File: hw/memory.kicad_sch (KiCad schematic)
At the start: 5 parts

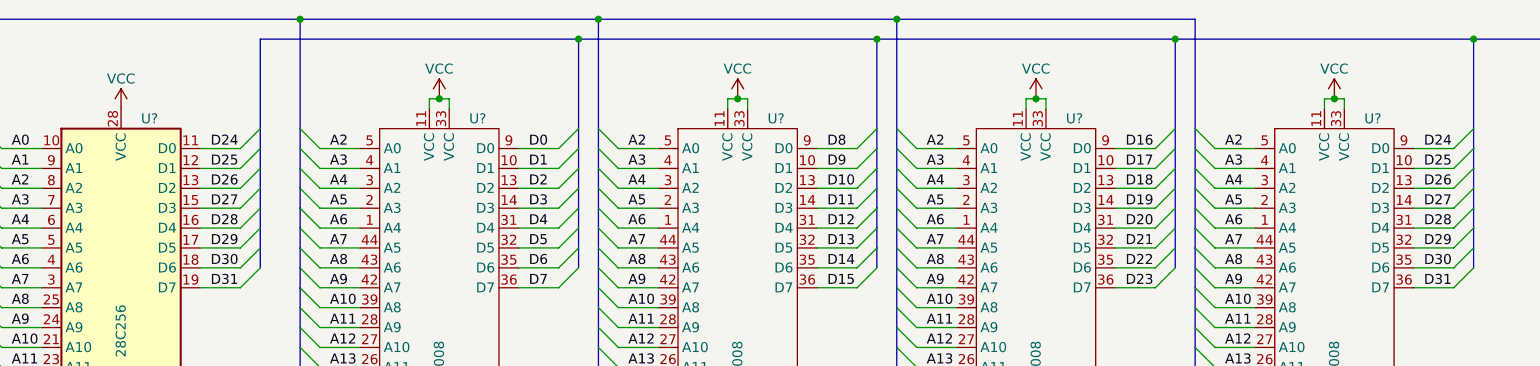
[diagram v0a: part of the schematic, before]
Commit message: fixed ERC errors
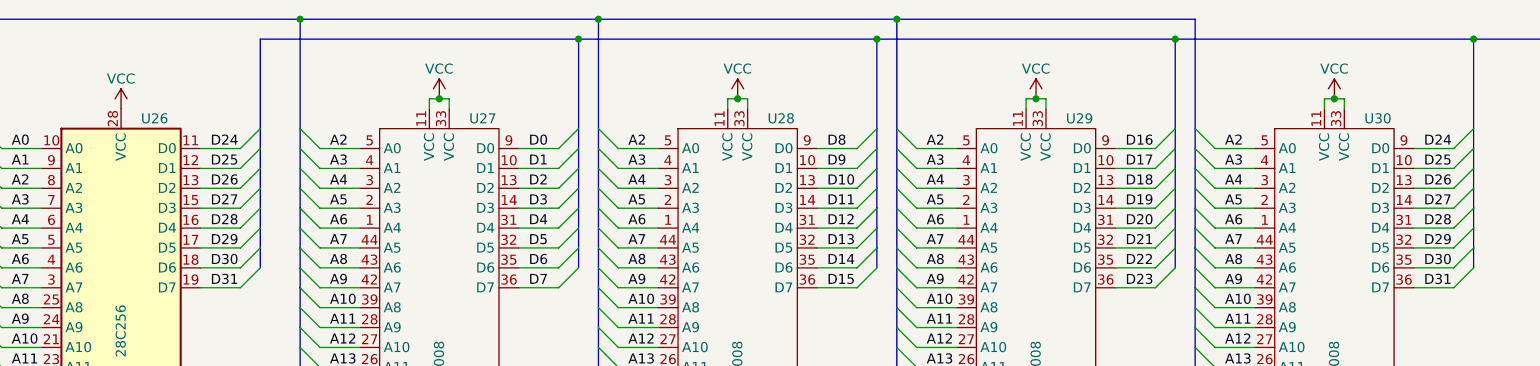
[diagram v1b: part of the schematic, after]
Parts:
- gave numbers to parts that had none: 5
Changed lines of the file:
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@@
   (symbol (lib_id "power:VCC") (at 135.89 101.6 0) (unit 1)
     (in_bom yes) (on_board yes)
-    (property "Reference" "#PWR?" (id 0) (at 135.89 105.41 0)
+    (property "Reference" "#PWR072" (id 0) (at 135.89 105.41 0)
       (effects (font (size 1.27 1.27)) hide)
     )
@@
   (symbol (lib_id "power:VCC") (at 212.09 101.6 0) (unit 1)
     (in_bom yes) (on_board yes)
-    (property "Reference" "#PWR?" (id 0) (at 212.09 105.41 0)
+    (property "Reference" "#PWR078" (id 0) (at 212.09 105.41 0)
       (effects (font (size 1.27 1.27)) hide)
     )
@@
   (symbol (lib_id "power:VCC") (at 173.99 101.6 0) (unit 1)
     (in_bom yes) (on_board yes)
-    (property "Reference" "#PWR?" (id 0) (at 173.99 105.41 0)
+    (property "Reference" "#PWR075" (id 0) (at 173.99 105.41 0)
       (effects (font (size 1.27 1.27)) hide)
     )
@@
   (symbol (lib_id "m68kcomp2:as6c8008") (at 110.49 71.12 0) (unit 1)
     (in_bom yes) (on_board yes)
-    (property "Reference" "U?" (id 0) (at 114.3 39.37 0)
+    (property "Reference" "U27" (id 0) (at 114.3 39.37 0)
       (effects (font (size 1.27 1.27)) (justify left))
     )
@@
   (symbol (lib_id "power:GND") (at 110.49 105.41 0) (unit 1)
     (in_bom yes) (on_board yes)
-    (property "Reference" "#PWR?" (id 0) (at 110.49 111.76 0)
+    (property "Reference" "#PWR071" (id 0) (at 110.49 111.76 0)
       (effects (font (size 1.27 1.27)) hide)
     )
@@
   (symbol (lib_id "power:GND") (at 148.59 105.41 0) (unit 1)
     (in_bom yes) (on_board yes)
-    (property "Reference" "#PWR?" (id 0) (at 148.59 111.76 0)
+    (property "Reference" "#PWR074" (id 0) (at 148.59 111.76 0)
       (effects (font (size 1.27 1.27)) hide)
     )
@@
   (symbol (lib_id "power:GND") (at 224.79 105.41 0) (unit 1)
     (in_bom yes) (on_board yes)
-    (property "Reference" "#PWR?" (id 0) (at 224.79 111.76 0)
+    (property "Reference" "#PWR080" (id 0) (at 224.79 111.76 0)
       (effects (font (size 1.27 1.27)) hide)
     )
@@
   (symbol (lib_id "power:VCC") (at 97.79 101.6 0) (unit 1)
     (in_bom yes) (on_board yes)
-    (property "Reference" "#PWR?" (id 0) (at 97.79 105.41 0)
+    (property "Reference" "#PWR069" (id 0) (at 97.79 105.41 0)
       (effects (font (size 1.27 1.27)) hide)
     )
@@
   (symbol (lib_id "Memory_EEPROM:28C256") (at 69.85 66.04 0) (unit 1)
     (in_bom yes) (on_board yes)
-    (property "Reference" "U?" (id 0) (at 72.39 39.37 0)
+    (property "Reference" "U26" (id 0) (at 72.39 39.37 0)
       (effects (font (size 1.27 1.27)) (justify left))
     )
@@
   (symbol (lib_id "power:VCC") (at 186.69 36.83 0) (unit 1)
     (in_bom yes) (on_board yes)
-    (property "Reference" "#PWR?" (id 0) (at 186.69 40.64 0)
+    (property "Reference" "#PWR076" (id 0) (at 186.69 40.64 0)
       (effects (font (size 1.27 1.27)) hide)
     )
@@
   (symbol (lib_id "m68kcomp2:as6c8008") (at 224.79 71.12 0) (unit 1)
     (in_bom yes) (on_board yes)
-    (property "Reference" "U?" (id 0) (at 228.6 39.37 0)
+    (property "Reference" "U30" (id 0) (at 228.6 39.37 0)
       (effects (font (size 1.27 1.27)) (justify left))
     )
@@
   (symbol (lib_id "power:VCC") (at 58.42 83.82 0) (unit 1)
     (in_bom yes) (on_board yes)
-    (property "Reference" "#PWR?" (id 0) (at 58.42 87.63 0)
+    (property "Reference" "#PWR066" (id 0) (at 58.42 87.63 0)
       (effects (font (size 1.27 1.27)) hide)
     )
@@
   (symbol (lib_id "power:VCC") (at 69.85 38.1 0) (unit 1)
     (in_bom yes) (on_board yes)
-    (property "Reference" "#PWR?" (id 0) (at 69.85 41.91 0)
+    (property "Reference" "#PWR067" (id 0) (at 69.85 41.91 0)
       (effects (font (size 1.27 1.27)) hide)
     )
@@
   (symbol (lib_id "power:VCC") (at 224.79 36.83 0) (unit 1)
     (in_bom yes) (on_board yes)
-    (property "Reference" "#PWR?" (id 0) (at 224.79 40.64 0)
+    (property "Reference" "#PWR079" (id 0) (at 224.79 40.64 0)
       (effects (font (size 1.27 1.27)) hide)
     )
@@
   (symbol (lib_id "power:GND") (at 69.85 93.98 0) (unit 1)
     (in_bom yes) (on_board yes)
-    (property "Reference" "#PWR?" (id 0) (at 69.85 100.33 0)
+    (property "Reference" "#PWR068" (id 0) (at 69.85 100.33 0)
       (effects (font (size 1.27 1.27)) hide)
     )
@@
   (symbol (lib_id "power:VCC") (at 110.49 36.83 0) (unit 1)
     (in_bom yes) (on_board yes)
-    (property "Reference" "#PWR?" (id 0) (at 110.49 40.64 0)
+    (property "Reference" "#PWR070" (id 0) (at 110.49 40.64 0)
       (effects (font (size 1.27 1.27)) hide)
     )
@@
   (symbol (lib_id "m68kcomp2:as6c8008") (at 148.59 71.12 0) (unit 1)
     (in_bom yes) (on_board yes)
-    (property "Reference" "U?" (id 0) (at 152.4 39.37 0)
+    (property "Reference" "U28" (id 0) (at 152.4 39.37 0)
       (effects (font (size 1.27 1.27)) (justify left))
     )
@@
   (symbol (lib_id "power:GND") (at 186.69 105.41 0) (unit 1)
     (in_bom yes) (on_board yes)
-    (property "Reference" "#PWR?" (id 0) (at 186.69 111.76 0)
+    (property "Reference" "#PWR077" (id 0) (at 186.69 111.76 0)
       (effects (font (size 1.27 1.27)) hide)
     )
@@
   (symbol (lib_id "power:VCC") (at 148.59 36.83 0) (unit 1)
     (in_bom yes) (on_board yes)
-    (property "Reference" "#PWR?" (id 0) (at 148.59 40.64 0)
+    (property "Reference" "#PWR073" (id 0) (at 148.59 40.64 0)
       (effects (font (size 1.27 1.27)) hide)
     )
@@
   (symbol (lib_id "m68kcomp2:as6c8008") (at 186.69 71.12 0) (unit 1)
     (in_bom yes) (on_board yes)
-    (property "Reference" "U?" (id 0) (at 190.5 39.37 0)
-      (effects (font (size 1.27 1.27)) (justify left))
-    )
+    (property "Reference" "U29" (id 0) (at 190.5 39.37 0)
+      (effects (font (size 1.27 1.27)) (justify left))
+    )
